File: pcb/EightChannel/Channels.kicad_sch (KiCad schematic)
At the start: 24 parts, among them J105 Strip 0, J106 Strip 1, J107 Strip 2, J108 Strip 3, J109 Strip 4, J110 Strip 5, J111 Strip 6, J112 Strip 7

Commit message: Intermediate
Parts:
- J201: renamed from J105; footprint (none) -> advent_sternla:CONN_ANGLED_4_2.54
- J202: renamed from J107; footprint (none) -> advent_sternla:CONN_ANGLED_4_2.54
- J203: renamed from J109; footprint (none) -> advent_sternla:CONN_ANGLED_4_2.54
- J204: renamed from J111; footprint (none) -> advent_sternla:CONN_ANGLED_4_2.54
- J205: renamed from J106; footprint (none) -> advent_sternla:CONN_ANGLED_4_2.54
- J206: renamed from J108; footprint (none) -> advent_sternla:CONN_ANGLED_4_2.54
- J207: renamed from J110; footprint (none) -> advent_sternla:CONN_ANGLED_4_2.54
- J208: renamed from J112; footprint (none) -> advent_sternla:CONN_ANGLED_4_2.54
- renumbered R103 to R201, R105 to R202, R107 to R203, R109 to R204, R111 to R205, R113 to R206, R115 to R207, R117 to R208, R102 to R209, R104 to R210, R106 to R211, R108 to R212, R110 to R213, R112 to R214, R114 to R215, R116 to R216

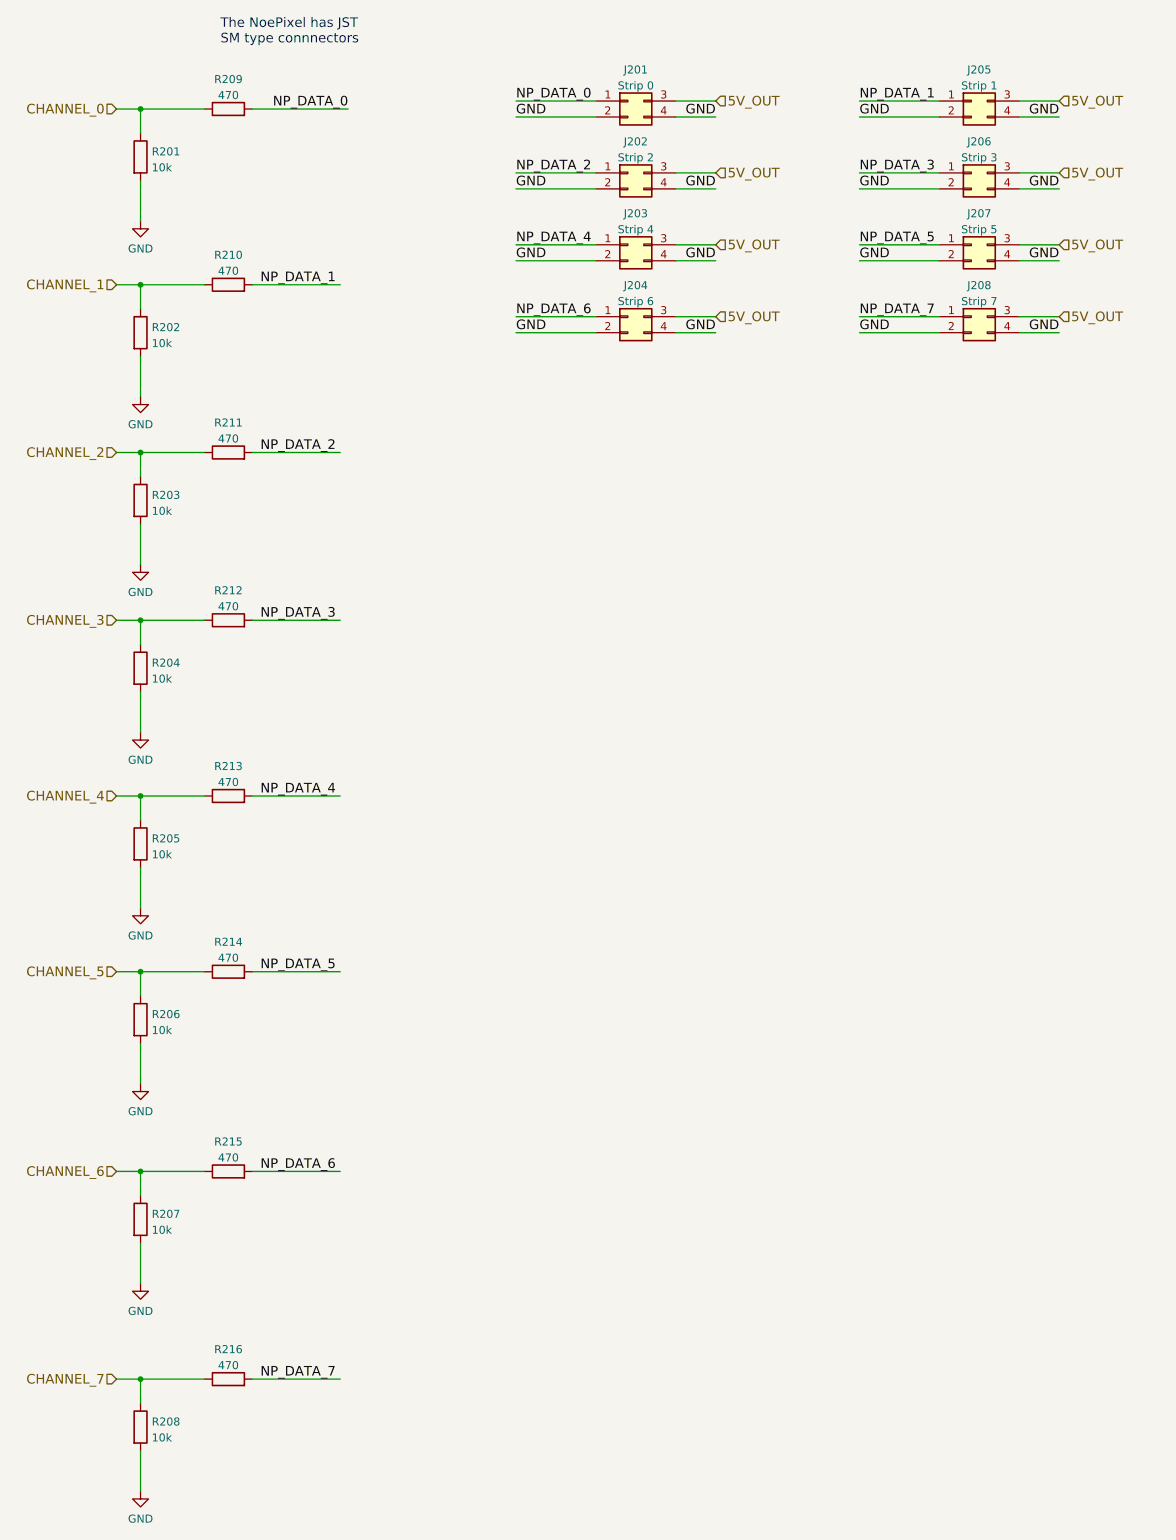
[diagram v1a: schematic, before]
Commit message: Finished 8Channel and submitted to Fab
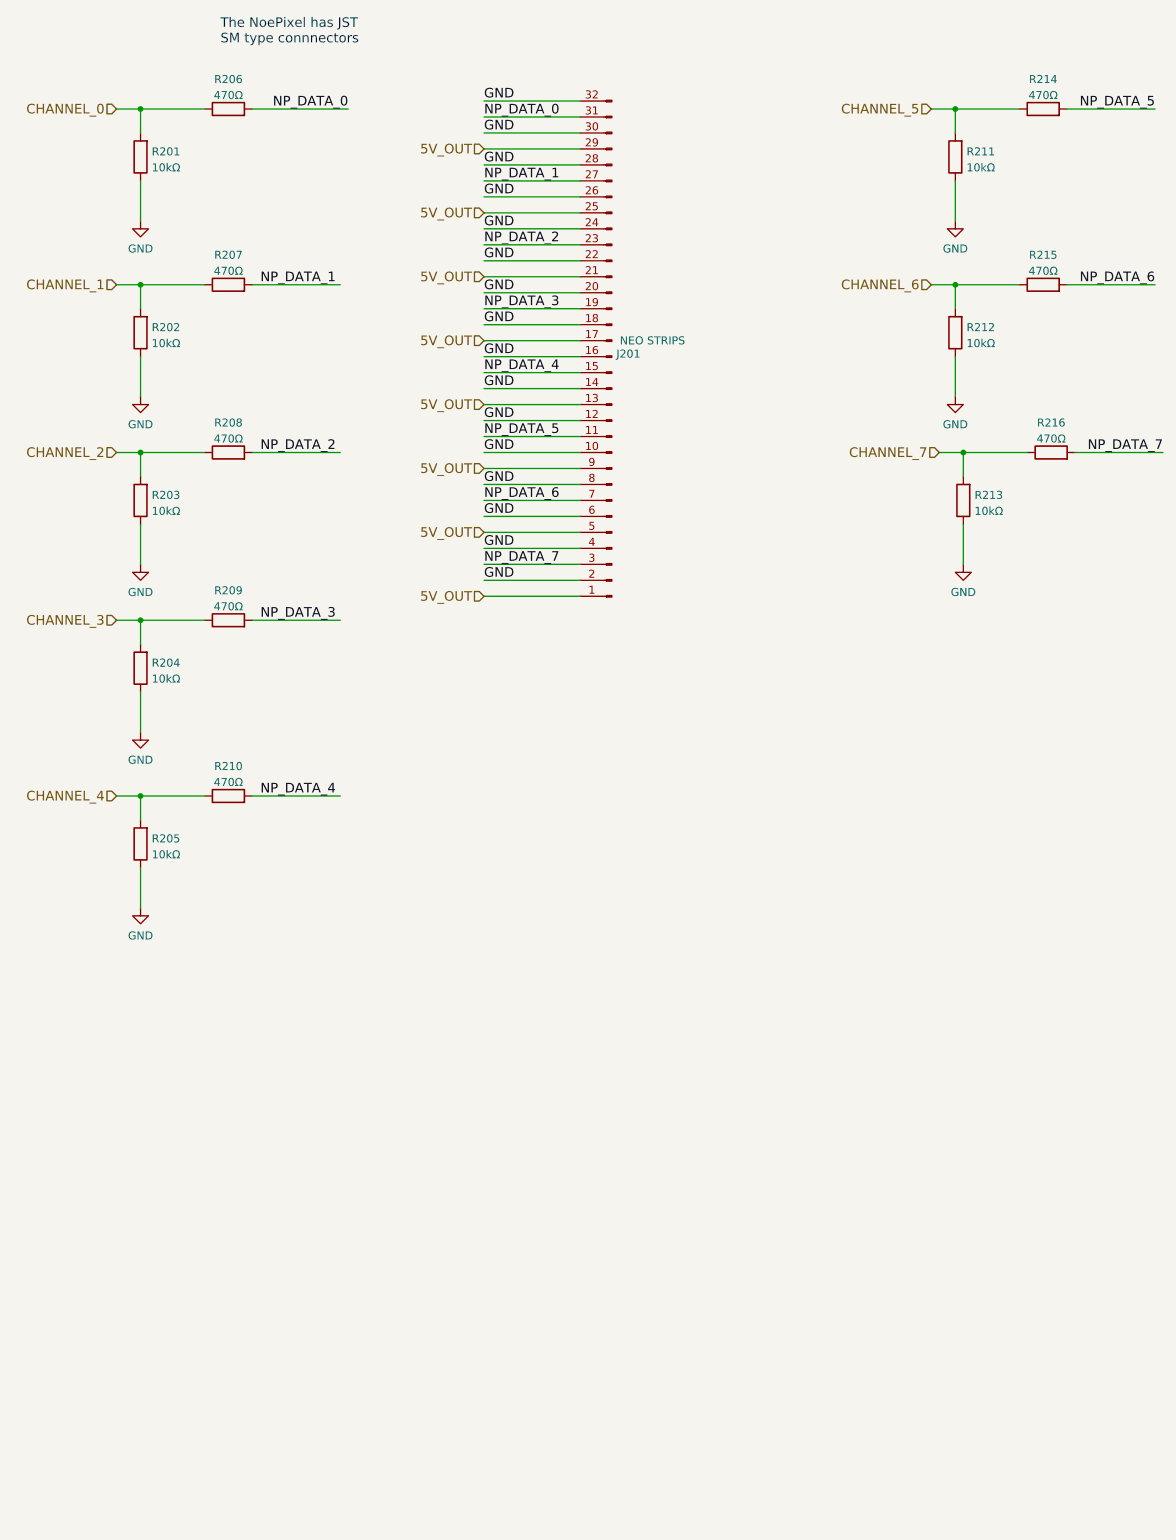
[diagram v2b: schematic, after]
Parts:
- removed J201: Strip 0, advent_sternla:CONN_ANGLED_4_2.54, symbol Connector_Generic:Conn_02x02_Top_Bottom
- removed J202: Strip 2, advent_sternla:CONN_ANGLED_4_2.54, symbol Connector_Generic:Conn_02x02_Top_Bottom
- removed J203: Strip 4, advent_sternla:CONN_ANGLED_4_2.54, symbol Connector_Generic:Conn_02x02_Top_Bottom
- removed J204: Strip 6, advent_sternla:CONN_ANGLED_4_2.54, symbol Connector_Generic:Conn_02x02_Top_Bottom
- removed J205: Strip 1, advent_sternla:CONN_ANGLED_4_2.54, symbol Connector_Generic:Conn_02x02_Top_Bottom
- removed J206: Strip 3, advent_sternla:CONN_ANGLED_4_2.54, symbol Connector_Generic:Conn_02x02_Top_Bottom
- removed J207: Strip 5, advent_sternla:CONN_ANGLED_4_2.54, symbol Connector_Generic:Conn_02x02_Top_Bottom
- removed J208: Strip 7, advent_sternla:CONN_ANGLED_4_2.54, symbol Connector_Generic:Conn_02x02_Top_Bottom
- added J201: NEO STRIPS, Connector_PinHeader_2.54mm:PinHeader_2x16_P2.54mm_Horizontal, symbol Connector:Conn_01x32_Male
- R201, R202, R203, R204, R205: value 10k -> 10kΩ
- R206, R207, R208: value 10k -> 470Ω
- R209, R210, R214, R215, R216: value 470 -> 470Ω
- R211, R212, R213: value 470 -> 10kΩ
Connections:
- net 5V_OUT: now also J201.1 (Pin_1), J201.13 (Pin_13), J201.17 (Pin_17), J201.21 (Pin_21), J201.25 (Pin_25), J201.29 (Pin_29), J201.5 (Pin_5), J201.9 (Pin_9)
- net CHANNEL_0: now also R201.2, R206.1; no longer R201.1, R209.1
- net CHANNEL_1: now also R202.2, R207.1; no longer R202.1, R210.1
- net CHANNEL_2: now also R203.2, R208.1; no longer R203.1, R211.1
- net CHANNEL_3: now also R204.2, R209.1; no longer R204.1, R212.1
- net CHANNEL_4: now also R205.2, R210.1; no longer R205.1, R213.1
- net CHANNEL_5: now also R211.2; no longer R206.1
- net CHANNEL_6: now also R212.2; no longer R207.1
- net CHANNEL_7: now also R213.2; no longer R208.1
- net GND: now also R201.1, R202.1, R203.1, R204.1, R205.1, R211.1, R212.1, R213.1, J201.10 (Pin_10), J201.12 (Pin_12), J201.14 (Pin_14), J201.16 (Pin_16), J201.18 (Pin_18), J201.2 (Pin_2), J201.20 (Pin_20), J201.22 (Pin_22), J201.24 (Pin_24), J201.26 (Pin_26), J201.28 (Pin_28), J201.30 (Pin_30), J201.32 (Pin_32), J201.4 (Pin_4), J201.6 (Pin_6), J201.8 (Pin_8); no longer R201.2, R202.2, R203.2, R204.2, R205.2, R206.2, R207.2, R208.2
- net NP_DATA_0: now also R206.2, J201.31 (Pin_31); no longer R209.2
- net NP_DATA_1: now also R207.2, J201.27 (Pin_27); no longer R210.2
- net NP_DATA_2: now also R208.2, J201.23 (Pin_23); no longer R211.2
- net NP_DATA_3: now also R209.2, J201.19 (Pin_19); no longer R212.2
- net NP_DATA_4: now also R210.2, J201.15 (Pin_15); no longer R213.2
- net NP_DATA_5: now also J201.11 (Pin_11)
- net NP_DATA_6: now also J201.7 (Pin_7)
- net NP_DATA_7: now also J201.3 (Pin_3)

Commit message: Update and synch of the eight channel design
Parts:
- R201, R202, R203, R204, R205, R211, R212, R213: value 10kΩ -> 1kΩ
- R206, R207, R208, R209, R210, R214, R215, R216: value 470Ω -> 0Ω
